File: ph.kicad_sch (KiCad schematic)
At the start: 40 parts, among them IC2 ADUM6010ARSZ, J4 pH, U10 REF3020, U11 TPS60400DBV, U12 ADS1115IDGS, U13 ADuM1250, U14 TLV271, U15 TLV271

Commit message: Add title to all schematics pages
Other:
- title: (none) -> pH
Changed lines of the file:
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@@
 	(paper "A4")
 	(title_block
+		(title "pH")
 		(rev "1")
 	)

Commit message: Redesign board to fit within 102mm x 102mm
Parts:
- IC2, R26, U10, U11, U12, U13, U14, U15: now left out of the parts list
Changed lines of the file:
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@@
 		(unit 1)
 		(exclude_from_sim no)
-		(in_bom yes)
+		(in_bom no)
 		(on_board yes)
 		(dnp no)
@@
 		(unit 1)
 		(exclude_from_sim no)
-		(in_bom yes)
+		(in_bom no)
 		(on_board yes)
 		(dnp no)
@@
 		(unit 1)
 		(exclude_from_sim no)
-		(in_bom yes)
+		(in_bom no)
 		(on_board yes)
 		(dnp no)
@@
 		(unit 1)
 		(exclude_from_sim no)
-		(in_bom yes)
+		(in_bom no)
 		(on_board yes)
 		(dnp no)
@@
 		(unit 1)
 		(exclude_from_sim no)
-		(in_bom yes)
+		(in_bom no)
 		(on_board yes)
 		(dnp no)
@@
 		(unit 1)
 		(exclude_from_sim no)
-		(in_bom yes)
+		(in_bom no)
 		(on_board yes)
 		(dnp no)
@@
 		(unit 1)
 		(exclude_from_sim no)
-		(in_bom yes)
+		(in_bom no)
 		(on_board yes)
 		(dnp no)
@@
 		(unit 1)
 		(exclude_from_sim no)
-		(in_bom yes)
+		(in_bom no)
 		(on_board yes)
 		(dnp no)

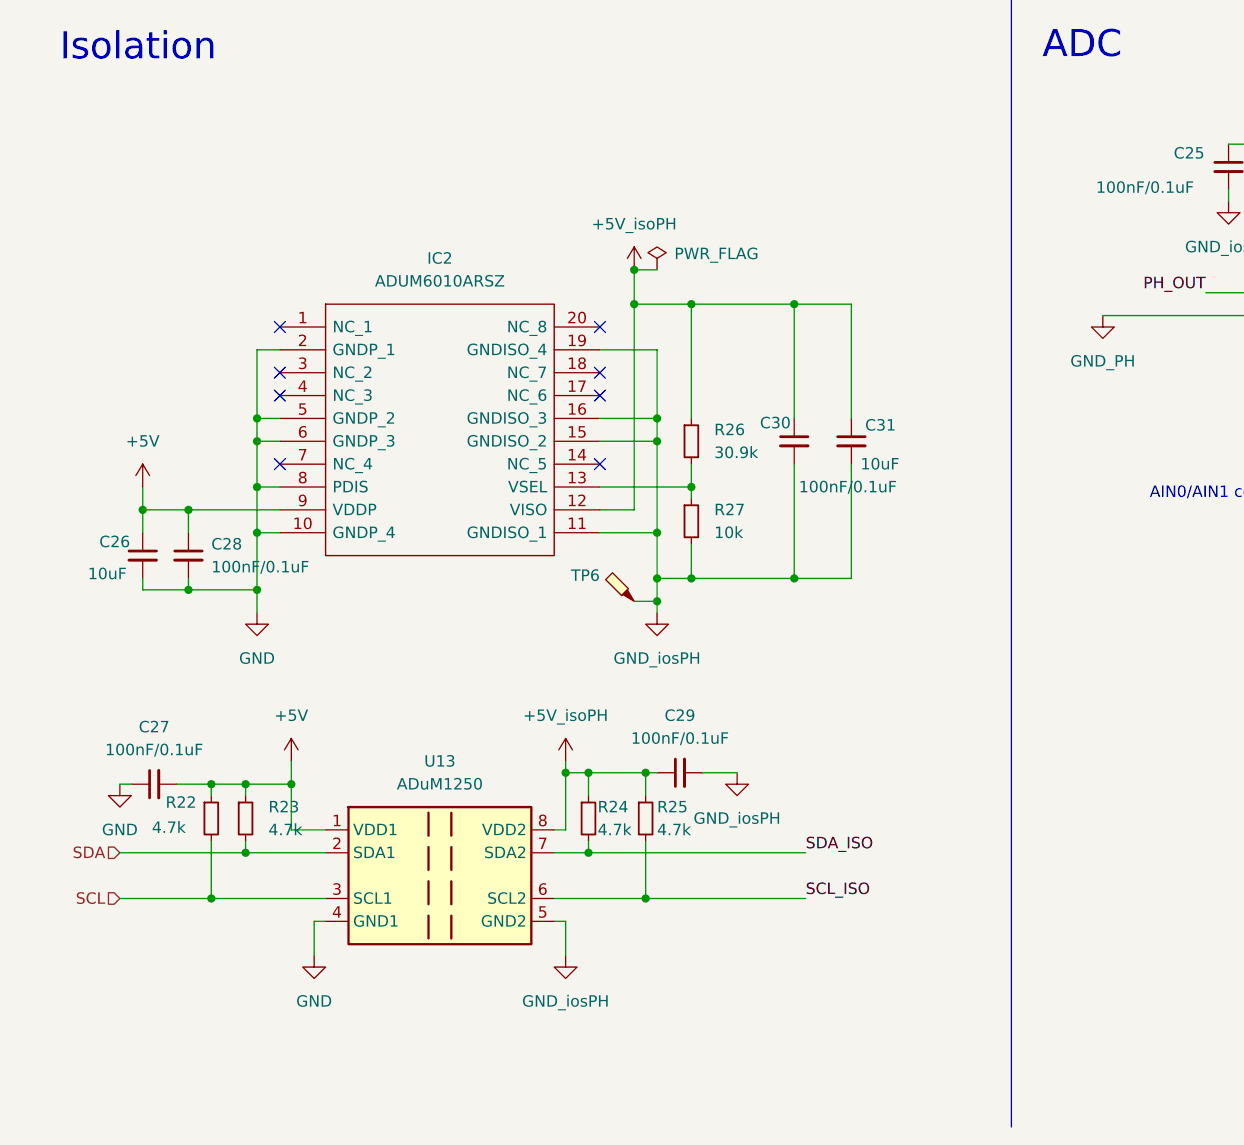
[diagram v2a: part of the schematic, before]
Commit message: Switch isolators to ADM3260
Change pH isolator
Closes #1
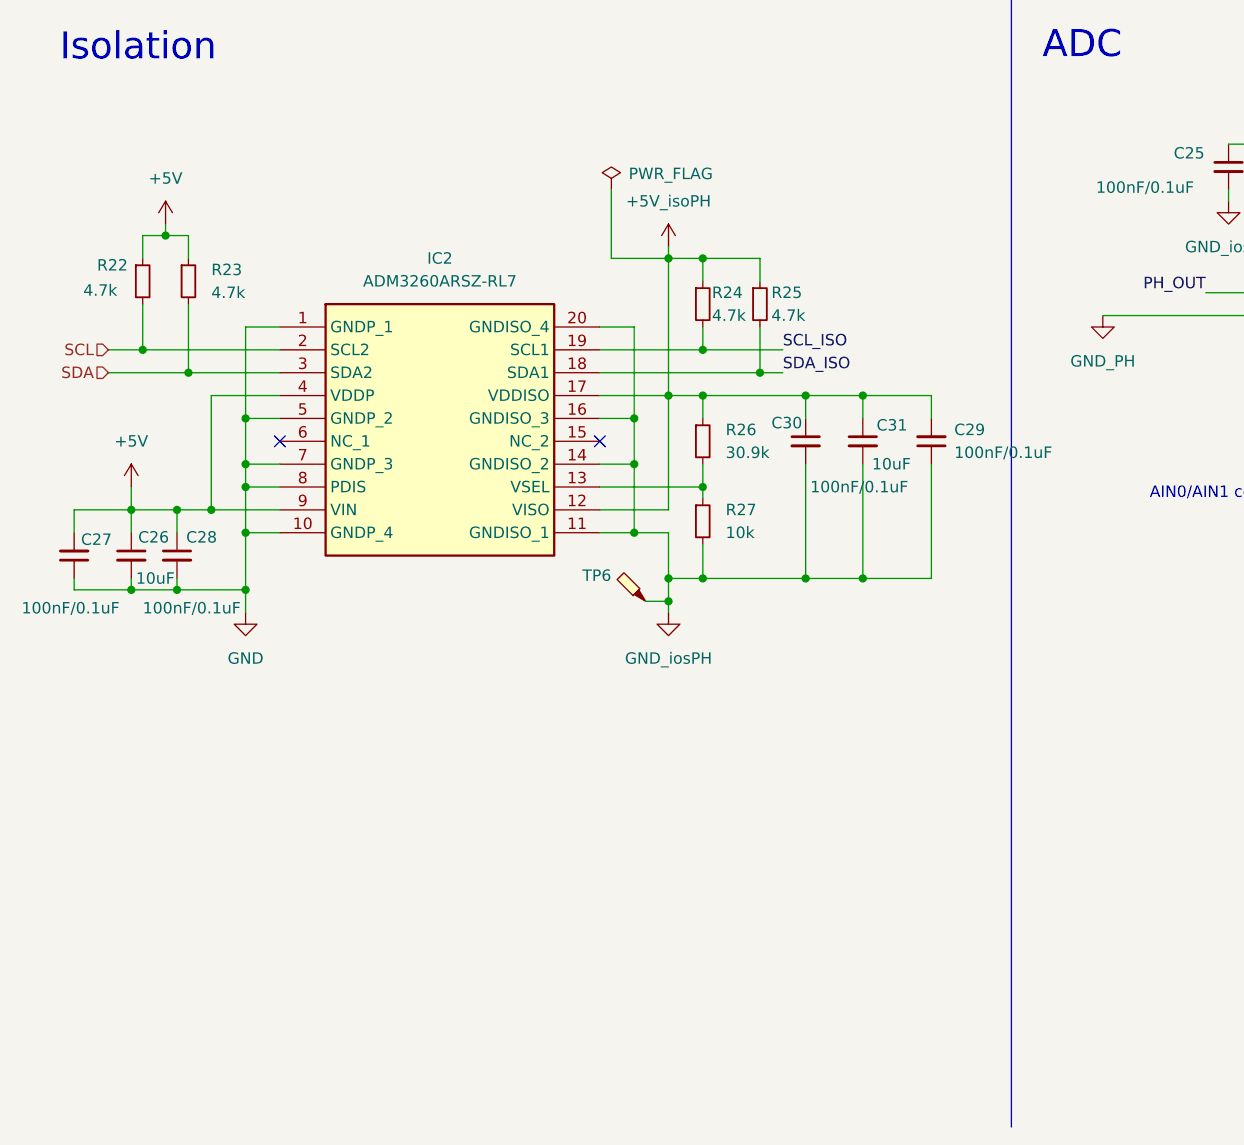
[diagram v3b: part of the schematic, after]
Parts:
- removed IC2: ADUM6010ARSZ, HydroponicFlowerControl:ADUM6010, symbol HydroponicFlowerControl:ADUM6010ARSZ
- removed U13: ADuM1250, Package_SO:SOIC-8_3.9x4.9mm_P1.27mm, symbol Isolator:ADuM1250
- added IC2: ADM3260ARSZ-RL7, HydroponicFlowerControl:SOP65P780X200-20N, symbol HydroponicFlowerControl:ADM3260ARSZ-RL7
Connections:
- net +5V: now also IC2.4 (VDDP), IC2.9 (VIN)
- net +5V_isoPH: now also C29.2, IC2.12 (VISO), IC2.17 (VDDISO); no longer C29.1
- net GND: now also IC2.1 (GNDP_1), IC2.10 (GNDP_4), IC2.5 (GNDP_2), IC2.7 (GNDP_3), IC2.8 (PDIS)
- net GND_iosPH: now also C29.1, IC2.11 (GNDISO_1), IC2.14 (GNDISO_2), IC2.16 (GNDISO_3), IC2.20 (GNDISO_4); no longer C29.2
- net SCL: now also IC2.2 (SCL2)
- net SCL_ISO: now also R24.2, IC2.19 (SCL1); no longer R25.2
- net SDA: now also IC2.3 (SDA2)
- net SDA_ISO: now also R25.2, IC2.18 (SDA1); no longer R24.2
- net at R26.2, R27.1: now also IC2.13 (VSEL)
- no-connect marks 11 -> 5
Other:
- moved on the sheet: C26, C27, C28, C29, C30, C31, R22, R23, R24, R25, R26, R27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

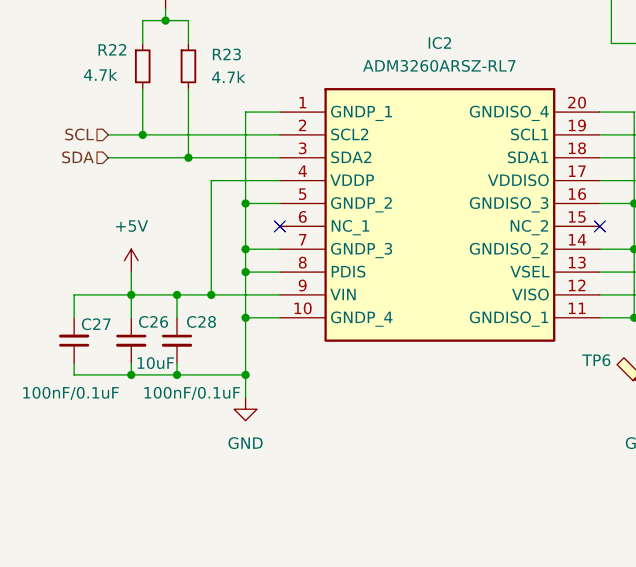
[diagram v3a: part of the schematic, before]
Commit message: Add disable signals for ec and ph
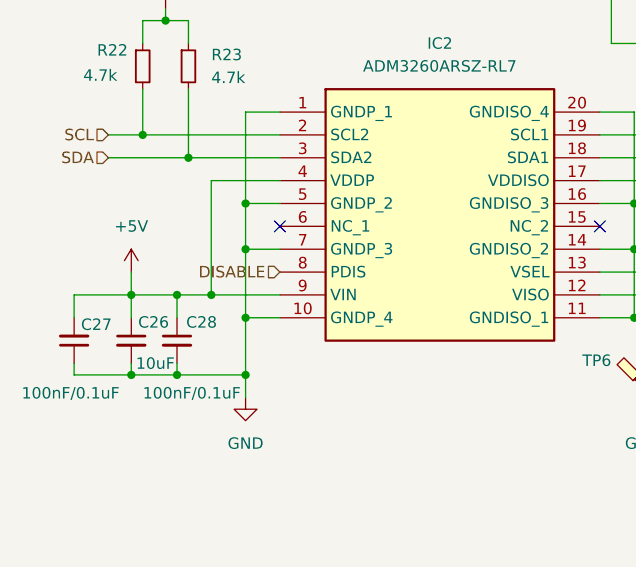
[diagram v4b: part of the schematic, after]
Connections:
- net GND: no longer IC2.8 (PDIS)
- new net DISABLE: IC2.8 (PDIS)
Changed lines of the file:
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@@
-	)
-	(junction
-		(at 36.83 127)
-		(diameter 0)
-		(color 0 0 0 0)
 	)
 	(junction
@@
 	(wire
 		(pts
-			(xy 36.83 127) (xy 40.64 127)
-		)
-		(stroke
-			(width 0)
-			(type default)
-		)
-	)
-	(wire
-		(pts
 			(xy 22.86 33.02) (xy 22.86 38.1)
 		)
@@
 	(wire
 		(pts
-			(xy 36.83 127) (xy 36.83 132.08)
+			(xy 36.83 124.46) (xy 36.83 132.08)
 		)
 		(stroke
@@
 		(pts
 			(xy 33.02 129.54) (xy 40.64 129.54)
-		)
-		(stroke
-			(width 0)
-			(type default)
-		)
-	)
-	(wire
-		(pts
-			(xy 36.83 124.46) (xy 36.83 127)
 		)
 		(stroke
@@
 		)
 	)
+	(hierarchical_label "DISABLE"
+		(shape input)
+		(at 40.64 127 180)
+		(fields_autoplaced yes)
+		(effects
+			(font
+				(size 1.27 1.27)
+			)
+			(justify right)
+		)
+	)

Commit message: Fix manufaturing properties
Such as rotations
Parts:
- IC2, U12: JLCPCB Rotation Offset (none) -> 270; now in the parts list
- R26, U10, U11, U14, U15: now in the parts list
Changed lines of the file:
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@@
 		(unit 1)
 		(exclude_from_sim no)
-		(in_bom no)
+		(in_bom yes)
 		(on_board yes)
 		(dnp no)
@@
 		(unit 1)
 		(exclude_from_sim no)
-		(in_bom no)
+		(in_bom yes)
 		(on_board yes)
 		(dnp no)
@@
 		(unit 1)
 		(exclude_from_sim no)
-		(in_bom no)
+		(in_bom yes)
 		(on_board yes)
 		(dnp no)
@@
 		(unit 1)
 		(exclude_from_sim no)
-		(in_bom no)
+		(in_bom yes)
 		(on_board yes)
 		(dnp no)
@@
 		(unit 1)
 		(exclude_from_sim no)
-		(in_bom no)
+		(in_bom yes)
 		(on_board yes)
 		(dnp no)
@@
 		(unit 1)
 		(exclude_from_sim no)
-		(in_bom no)
+		(in_bom yes)
 		(on_board yes)
 		(dnp no)
@@
 			)
 		)
+		(property "JLCPCB Rotation Offset" "270"
+			(at 160.02 107.95 0)
+			(effects
+				(font
+					(size 1.27 1.27)
+				)
+				(hide yes)
+			)
+		)
 		(pin "3"
 		)
@@
 		(unit 1)
 		(exclude_from_sim no)
-		(in_bom no)
+		(in_bom yes)
 		(on_board yes)
 		(dnp no)
@@
 				(hide yes)
 			)
+		)
+		(property "JLCPCB Rotation Offset" "270"
+			(at 40.64 109.22 0)
+			(effects
+				(font
+					(size 1.27 1.27)
+				)
+				(hide yes)
+			)

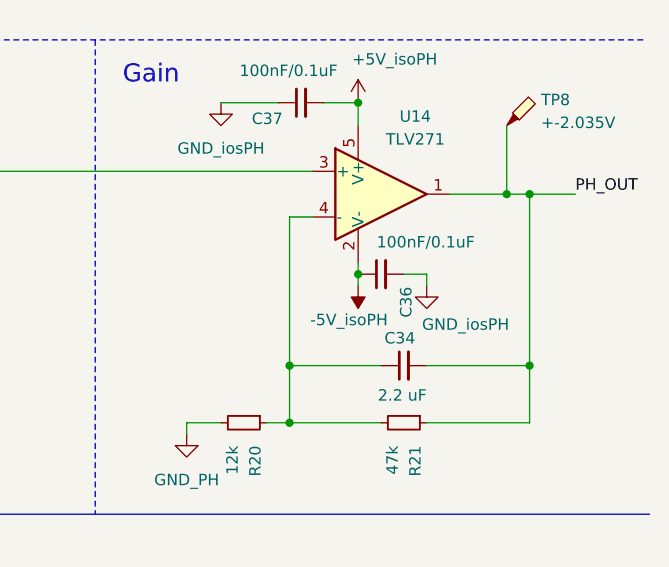
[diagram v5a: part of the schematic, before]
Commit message: Protect PH_OUT from going out of bounds
Closes #7
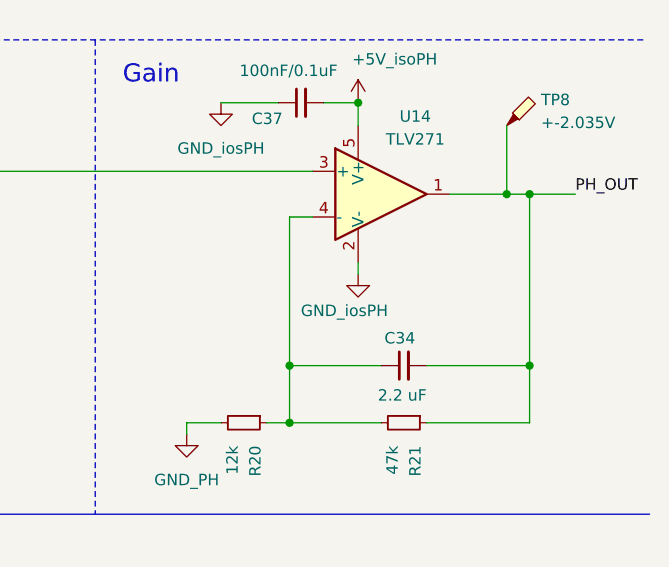
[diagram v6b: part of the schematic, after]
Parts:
- removed C36: 100nF/0.1uF, Capacitor_SMD:C_0603_1608Metric, symbol Device:C_Small
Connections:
- net -5V_isoPH: no longer U14.2 (V-)
- net GND_iosPH: now also U14.2 (V-)
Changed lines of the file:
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@@
 	)
 	(junction
-		(at 252.73 45.72)
-		(diameter 0)
-		(color 0 0 0 0)
-	)
-	(junction
 		(at 93.98 114.3)
 		(diameter 0)
@@
 	(wire
 		(pts
-			(xy 252.73 45.72) (xy 252.73 46.99)
-		)
-		(stroke
-			(width 0)
-			(type default)
-		)
-	)
-	(wire
-		(pts
 			(xy 99.06 119.38) (xy 99.06 116.84)
 		)
@@
 	(wire
 		(pts
-			(xy 257.81 45.72) (xy 260.35 45.72)
-		)
-		(stroke
-			(width 0)
-			(type default)
-		)
-	)
-	(wire
-		(pts
 			(xy 83.82 137.16) (xy 83.82 139.7)
 		)
@@
 	(wire
 		(pts
-			(xy 260.35 45.72) (xy 260.35 46.99)
-		)
-		(stroke
-			(width 0)
-			(type default)
-		)
-	)
-	(wire
-		(pts
 			(xy 171.45 44.45) (xy 172.72 44.45)
 		)
@@
 	(symbol
 		(lib_id "Device:C_Small")
-		(at 255.27 45.72 90)
-		(unit 1)
-		(exclude_from_sim no)
-		(in_bom yes)
-		(on_board yes)
-		(dnp no)
-		(property "Reference" "C36"
-			(at 258.064 50.546 0)
-			(effects
-				(font
-					(size 1.27 1.27)
-				)
-				(justify left)
-			)
-		)
-		(property "Value" "100nF/0.1uF"
-			(at 265.684 42.164 90)
-			(effects
-				(font
-					(size 1.27 1.27)
-				)
-				(justify left)
-			)
-		)
-		(property "Footprint" "Capacitor_SMD:C_0603_1608Metric"
-			(at 255.27 45.72 0)
-			(effects
-				(font
-					(size 1.27 1.27)
-				)
-				(hide yes)
-			)
-		)
-		(property "Datasheet" "~"
-			(at 255.27 45.72 0)
-			(effects
-				(font
-					(size 1.27 1.27)
-				)
-				(hide yes)
-			)
-		)
-		(property "Description" "Unpolarized capacitor, small symbol"
-			(at 255.27 45.72 0)
-			(effects
-				(font
-					(size 1.27 1.27)
-				)
-				(hide yes)
-			)
-		)
-		(property "LCSC" "C14663"
-			(at 255.27 45.72 0)
-			(effects
-				(font
-					(size 1.27 1.27)
-				)
-				(hide yes)
-			)
-		)
-		(property "LCSC alt" ""
-			(at 255.27 45.72 0)
-			(effects
-				(font
-					(size 1.27 1.27)
-				)
-				(hide yes)
-			)
-		)
-		(pin "2"
-		)
-		(pin "1"
-		)
-		(instances
-			(project "HydroponicFlowerControl"
-				(path "/b3c8a28b-9ce1-4002-b8e8-ef8cb73fe031/98c7b1ae-5b10-4cce-8f75-2d85473487c0"
-					(reference "C36")
-					(unit 1)
-				)
-			)
-		)
-	)
-	(symbol
-		(lib_id "Device:C_Small")
 		(at 17.78 134.62 180)
 		(unit 1)
@@
 	)
 	(symbol
-		(lib_id "power:-5VA")
-		(at 252.73 46.99 180)
-		(unit 1)
-		(exclude_from_sim no)
-		(in_bom yes)
-		(on_board yes)
-		(dnp no)
-		(property "Reference" "#PWR075"
-			(at 252.73 43.18 0)
-			(effects
-				(font
-					(size 1.27 1.27)
-				)
-				(hide yes)
-			)
-		)
-		(property "Value" "-5V_isoPH"
-			(at 251.714 50.8 0)
-			(effects
-				(font
-					(size 1.27 1.27)
-				)
-			)
-		)
-		(property "Footprint" ""
-			(at 252.73 46.99 0)
-			(effects
-				(font
-					(size 1.27 1.27)
-				)
-				(hide yes)
-			)
-		)
-		(property "Datasheet" ""
-			(at 252.73 46.99 0)
-			(effects
-				(font
-					(size 1.27 1.27)
-				)
-				(hide yes)
-			)
-		)
-		(property "Description" "Power symbol creates a global label with name \"-5VA\""
-			(at 252.73 46.99 0)
-			(effects
-				(font
-					(size 1.27 1.27)
-				)
-				(hide yes)
-			)
-		)
-		(pin "1"
-		)
-		(instances
-			(project "HydroponicFlowerControl"
-				(path "/b3c8a28b-9ce1-4002-b8e8-ef8cb73fe031/98c7b1ae-5b10-4cce-8f75-2d85473487c0"
-					(reference "#PWR075")
-					(unit 1)
-				)
-			)
-		)
-	)
-	(symbol
 		(lib_id "Device:C_Small")
 		(at 53.34 45.72 0)
@@
 	)
 	(symbol
+		(lib_id "power:GNDA")
+		(at 252.73 45.72 0)
+		(unit 1)
+		(exclude_from_sim no)
+		(in_bom yes)
+		(on_board yes)
+		(dnp no)
+		(property "Reference" "#PWR061"
+			(at 252.73 52.07 0)
+			(effects
+				(font
+					(size 1.27 1.27)
+				)
+				(hide yes)
+			)
+		)
+		(property "Value" "GND_iosPH"
+			(at 251.206 49.784 0)
+			(effects
+				(font
+					(size 1.27 1.27)
+				)
+			)
+		)
+		(property "Footprint" ""
+			(at 252.73 45.72 0)
+			(effects
+				(font
+					(size 1.27 1.27)
+				)
+				(hide yes)
+			)
+		)
+		(property "Datasheet" ""
+			(at 252.73 45.72 0)
+			(effects
+				(font
+					(size 1.27 1.27)
+				)
+				(hide yes)
+			)
+		)
+		(property "Description" "Power symbol creates a global label with name \"GNDA\" , analog ground"
+			(at 252.73 45.72 0)
+			(effects
+				(font
+					(size 1.27 1.27)
+				)
+				(hide yes)
+			)
+		)
+		(pin "1"
+		)
+		(instances
+			(project "HydroponicFlowerControl"
+				(path "/b3c8a28b-9ce1-4002-b8e8-ef8cb73fe031/98c7b1ae-5b10-4cce-8f75-2d85473487c0"
+					(reference "#PWR061")
+					(unit 1)
+				)
+			)
+		)
+	)
+	(symbol
 		(lib_id "Device:R_Small")
 		(at 87.63 106.68 0)
@@
 					(unit 1)
 				)
-			)
-		)
-	)
-	(symbol
-		(lib_id "power:GNDA")
-		(at 260.35 46.99 0)
-		(unit 1)
-		(exclude_from_sim no)
-		(in_bom yes)
-		(on_board yes)
-		(dnp no)
-		(property "Reference" "#PWR076"
-			(at 260.35 53.34 0)
-			(effects
-				(font
-					(size 1.27 1.27)
-				)
-				(hide yes)
-			)
-		)
-		(property "Value" "GND_iosPH"
-			(at 264.668 51.308 0)
-			(effects
-				(font
-					(size 1.27 1.27)
-				)
-			)
-		)
-		(property "Footprint" ""
-			(at 260.35 46.99 0)
-			(effects
-				(font
-					(size 1.27 1.27)
-				)
-				(hide yes)
-			)
-		)
-		(property "Datasheet" ""
-			(at 260.35 46.99 0)
-			(effects
-				(font
-					(size 1.27 1.27)
-				)
-				(hide yes)
-			)
-		)
-		(property "Description" "Power symbol creates a global label with name \"GNDA\" , analog ground"
-			(at 260.35 46.99 0)
-			(effects
-				(font
-					(size 1.27 1.27)
-				)
-				(hide yes)
-			)
-		)
-		(pin "1"
-		)
-		(instances
-			(project "HydroponicFlowerControl"
-				(path "/b3c8a28b-9ce1-4002-b8e8-ef8cb73fe031/98c7b1ae-5b10-4cce-8f75-2d85473487c0"
-					(reference "#PWR076")
-					(unit 1)
-				)

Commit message: Add testpoints for power and gnd
Closes #3
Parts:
- TP6, TP9: footprint TestPoint:TestPoint_Pad_D1.0mm -> TestPoint:TestPoint_Loop_D1.80mm_Drill1.0mm_Beaded; LCSC (none) -> C5199801
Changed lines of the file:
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@@
 			)
 		)
-		(property "Footprint" "TestPoint:TestPoint_Pad_D1.0mm"
+		(property "Footprint" "TestPoint:TestPoint_Loop_D1.80mm_Drill1.0mm_Beaded"
 			(at 76.2 139.7 0)
 			(effects
@@
 			)
 		)
-		(property "LCSC alt" ""
+		(property "LCSC" "C5199801"
 			(at 81.28 139.7 0)
 			(effects
@@
 			)
 		)
-		(property "Footprint" "TestPoint:TestPoint_Pad_D1.0mm"
+		(property "Footprint" "TestPoint:TestPoint_Loop_D1.80mm_Drill1.0mm_Beaded"
 			(at 127 39.37 0)
 			(effects
@@
 			)
 		)
-		(property "LCSC alt" ""
+		(property "LCSC" "C5199801"
 			(at 121.92 39.37 0)
 			(effects

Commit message: Align pH connector
See #10
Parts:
- TP7: value +-0.414V -> ±0.414V
- TP8: value +-2.035V -> ±2.035V
- TP9: footprint TestPoint:TestPoint_Loop_D1.80mm_Drill1.0mm_Beaded -> TestPoint:TestPoint_Pad_D1.0mm; LCSC C5199801 -> (none)
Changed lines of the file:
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@@
 		(on_board yes)
 		(dnp no)
-		(fields_autoplaced yes)
 		(property "Reference" "TP8"
 			(at 273.05 26.3524 0)
@@
 			)
 		)
-		(property "Value" "+-2.035V"
+		(property "Value" "±2.035V"
 			(at 273.05 28.8924 0)
 			(effects
@@
 			)
 		)
-		(property "Value" "+-0.414V"
+		(property "Value" "±0.414V"
 			(at 168.91 68.2624 0)
 			(effects
@@
 			)
 		)
-		(property "Footprint" "TestPoint:TestPoint_Loop_D1.80mm_Drill1.0mm_Beaded"
+		(property "Footprint" "TestPoint:TestPoint_Pad_D1.0mm"
 			(at 127 39.37 0)
 			(effects
@@
 			(at 121.92 39.37 0)
 			(effects
-				(font
-					(size 1.27 1.27)
-				)
-				(hide yes)
-			)
-		)
-		(property "LCSC" "C5199801"
-			(at 121.92 39.37 0)
-			(effects
